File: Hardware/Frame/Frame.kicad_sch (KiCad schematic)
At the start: 0 parts

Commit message: Made a regulator in kicad
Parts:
- added C1, C3: 100n, Capacitor_SMD:C_0402_1005Metric, symbol Device:C_Small
- added C2, C4, C5: 22u, Capacitor_SMD:CP_Elec_6.3x7.7, symbol Device:C_Polarized_Small
- added J3: Screw_Terminal_01x02, TerminalBlock_Phoenix:TerminalBlock_Phoenix_MKDS-1,5-2-5.08_1x02_P5.08mm_Horizontal, symbol Connector:Screw_Terminal_01x02
- added J4: USB_C_Receptacle_PowerOnly_6P, Connector_USB:USB_C_Receptacle_HRO_TYPE-C-31-M-12, symbol Connector:USB_C_Receptacle_PowerOnly_6P
- added R1, R2: 5.1k, Resistor_SMD:R_0402_1005Metric, symbol Device:R_Small
- added U1: AMS1117-1.8, Package_TO_SOT_SMD:SOT-223-3_TabPin2, symbol Regulator_Linear:AMS1117-1.8
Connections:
- new net: J4.B5 (CC2), R2.2
- new net: J4.A5 (CC1), R1.2
- new net +1.8V: C1.1, C2.1, C5.1, J3.1 (Pin_1), U1.2 (VO)
- new net +5VD: C3.1, C4.1, J4.A9 (VBUS), J4.B9 (VBUS), U1.3 (VI)
- new net GND: C1.2, C2.2, C3.2, C4.2, C5.2, J3.2 (Pin_2), J4.A12 (GND), J4.B12 (GND), J4.S1 (SHIELD), R1.1, R2.1, U1.1 (GND)

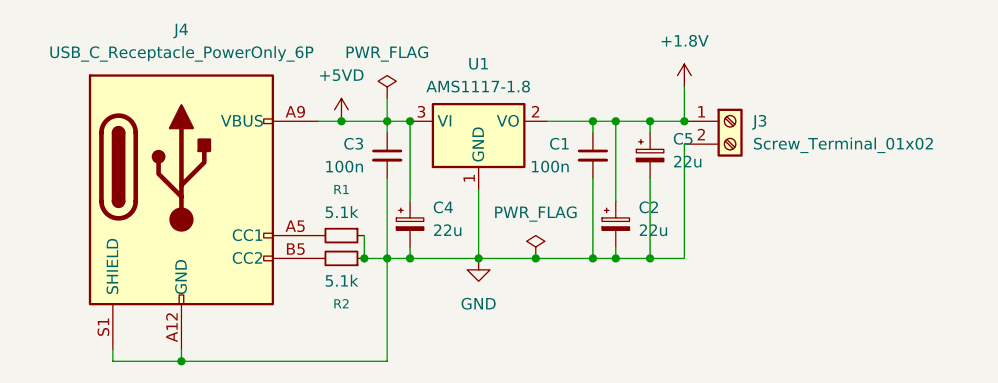
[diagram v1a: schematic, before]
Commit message: added glasses functionality.
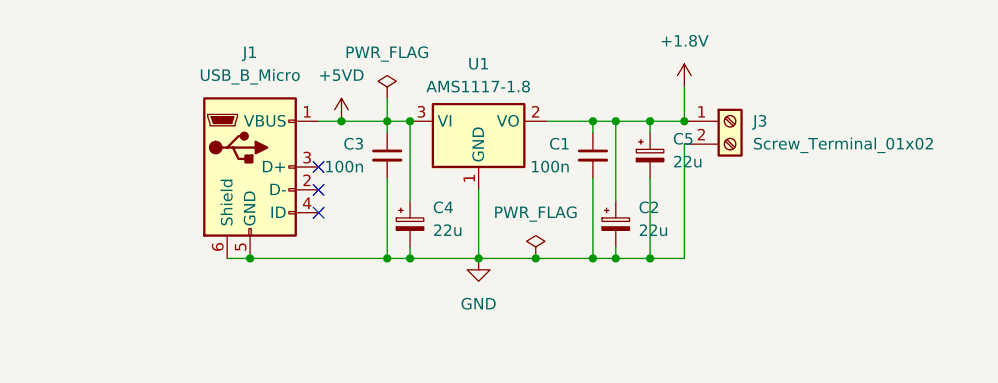
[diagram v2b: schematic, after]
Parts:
- removed J4: USB_C_Receptacle_PowerOnly_6P, Connector_USB:USB_C_Receptacle_HRO_TYPE-C-31-M-12, symbol Connector:USB_C_Receptacle_PowerOnly_6P
- removed R1, R2: 5.1k, Resistor_SMD:R_0402_1005Metric, symbol Device:R_Small
- added J1: USB_B_Micro, Connector_USB:USB_Micro-B_Amphenol_10118194_Horizontal, symbol Connector:USB_B_Micro
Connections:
- net +5VD: now also J1.1 (VBUS)
- net GND: now also J1.5 (GND), J1.6 (Shield)
- no-connect marks 0 -> 3
